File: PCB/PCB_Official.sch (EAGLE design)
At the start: 104 parts, among them IC1 MCP73871, J3 455-1750-1-ND, Q1 220mA/50V/3.5Ω, U1 TPS63070, U2 STM32F767ZIT6, U3 STM32L053C8T6, U4 TPS63070, U5 BATTERY-MANAGEMENT-TEMP_BQ274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

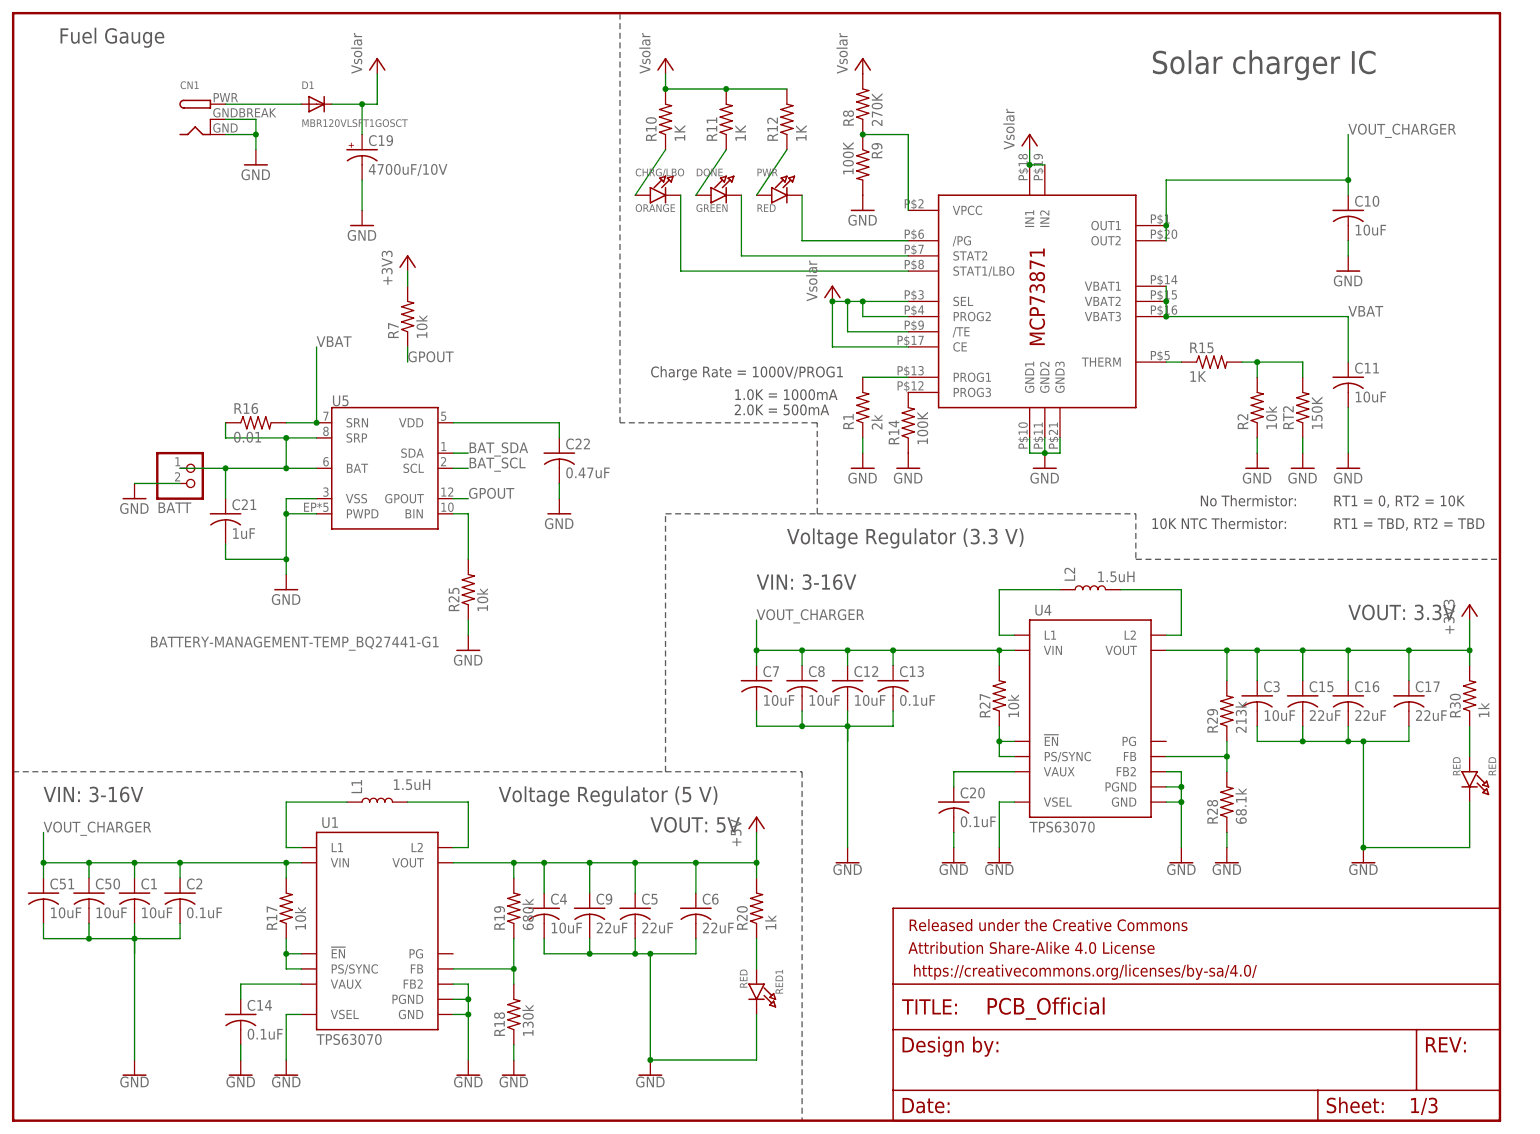
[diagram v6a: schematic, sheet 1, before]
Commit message: Passing DRU, need to fix silkscreen
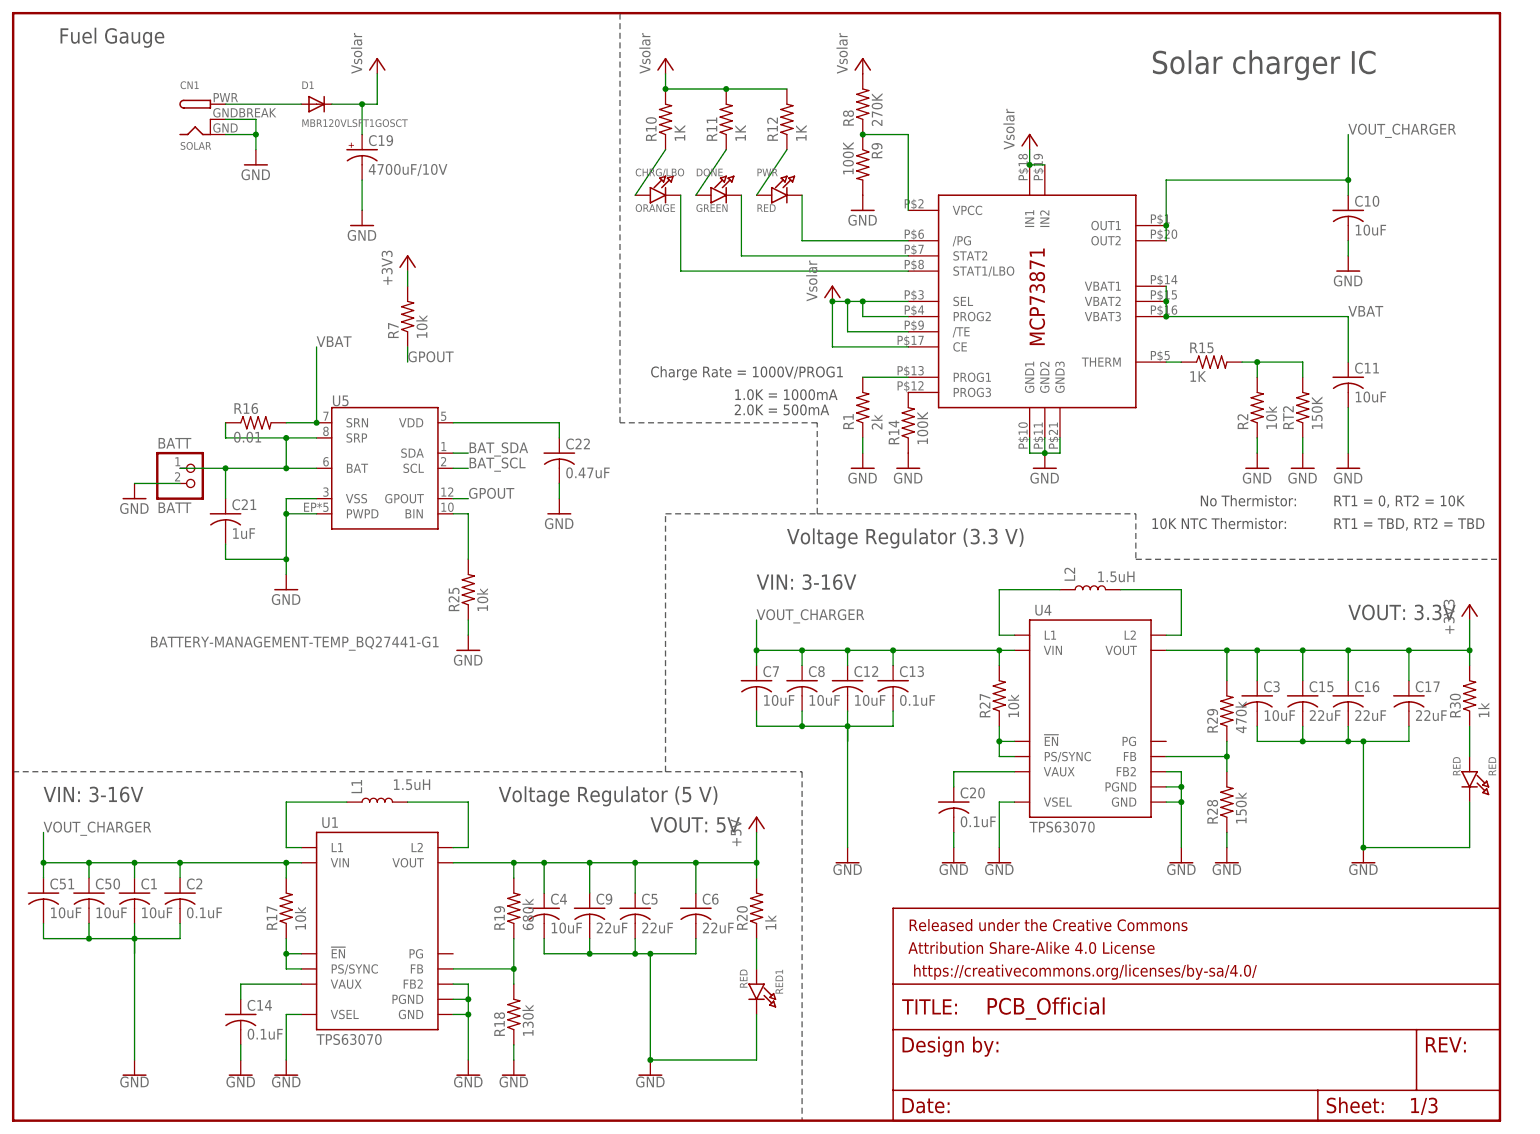
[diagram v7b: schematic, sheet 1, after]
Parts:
- BATT: value (none) -> BATT
- CN1: value (none) -> SOLAR
- J2: value (none) -> F7_PRGM
- L0_PROGRAM: value (none) -> L0_PRGM
- MCU_UART: value (none) -> MCU_UART
- R28: value 68.1k -> 150k
- R29: value 213k -> 470k
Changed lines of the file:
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@@
 <part name="GND13" library="supply1" deviceset="GND" device=""/>
 <part name="GND14" library="supply1" deviceset="GND" device=""/>
-<part name="BATT" library="adafruit" deviceset="JST_2PIN" device="-SMT-RA"/>
+<part name="BATT" library="adafruit" deviceset="JST_2PIN" device="-SMT-RA" value="BATT"/>
 <part name="GND15" library="supply1" deviceset="GND" device=""/>
 <part name="R14" library="adafruit" deviceset="R-US_" device="R0805" value="100K"/>
@@
 <part name="FRAME3" library="SparkFun-Aesthetics" library_urn="urn:adsk.eagle:library:507" deviceset="FRAME-LEDGER" device="" package3d_urn="urn:adsk.eagle:package:37121/1"/>
 <part name="U2" library="STM32F767ZIT6" deviceset="STM32F767ZIT6" device=""/>
-<part name="J2" library="SparkFun-Connectors" deviceset="CONN_05" device=""/>
+<part name="J2" library="SparkFun-Connectors" deviceset="CONN_05" device="" value="F7_PRGM"/>
 <part name="FRAME4" library="SparkFun-Aesthetics" library_urn="urn:adsk.eagle:library:507" deviceset="FRAME-A4L" device=""/>
 <part name="U3" library="STM32L053C8T6" deviceset="STM32L053C8T6" device=""/>
-<part name="L0_PROGRAM" library="SparkFun-Connectors" deviceset="CONN_05" device=""/>
+<part name="L0_PROGRAM" library="SparkFun-Connectors" deviceset="CONN_05" device="" value="L0_PRGM"/>
 <part name="U$9" library="ForestVisionParts" deviceset="LORAMODULE" device=""/>
 <part name="U$1" library="ForestVisionParts" deviceset="MIKROE_CLICK" device="LARGE"/>
@@
 <part name="C19" library="ForestVisionParts" deviceset="ADAFRUIT_CPOL-US" device="E5-13" value="4700uF/10V"/>
 <part name="GND43" library="supply1" deviceset="GND" device=""/>
-<part name="MCU_UART" library="pinhead" library_urn="urn:adsk.eagle:library:325" deviceset="PINHD-1X4" device="" package3d_urn="urn:adsk.eagle:package:22407/2"/>
+<part name="MCU_UART" library="pinhead" library_urn="urn:adsk.eagle:library:325" deviceset="PINHD-1X4" device="" package3d_urn="urn:adsk.eagle:package:22407/2" value="MCU_UART"/>
 <part name="C7" library="rcl" library_urn="urn:adsk.eagle:library:334" deviceset="C-US" device="C0603" package3d_urn="urn:adsk.eagle:package:23616/2" value="10uF"/>
 <part name="C20" library="rcl" library_urn="urn:adsk.eagle:library:334" deviceset="C-US" device="C0603" package3d_urn="urn:adsk.eagle:package:23616/2" value="0.1uF"/>
 <part name="R27" library="rcl" library_urn="urn:adsk.eagle:library:334" deviceset="R-US_" device="R0603" package3d_urn="urn:adsk.eagle:package:23555/3" value="10k"/>
-<part name="R28" library="rcl" library_urn="urn:adsk.eagle:library:334" deviceset="R-US_" device="R0603" package3d_urn="urn:adsk.eagle:package:23555/3" value="68.1k"/>
-<part name="R29" library="rcl" library_urn="urn:adsk.eagle:library:334" deviceset="R-US_" device="R0603" package3d_urn="urn:adsk.eagle:package:23555/3" value="213k"/>
+<part name="R28" library="rcl" library_urn="urn:adsk.eagle:library:334" deviceset="R-US_" device="R0603" package3d_urn="urn:adsk.eagle:package:23555/3" value="150k"/>
+<part name="R29" library="rcl" library_urn="urn:adsk.eagle:library:334" deviceset="R-US_" device="R0603" package3d_urn="urn:adsk.eagle:package:23555/3" value="470k"/>
 <part name="R30" library="rcl" library_urn="urn:adsk.eagle:library:334" deviceset="R-US_" device="R0603" package3d_urn="urn:adsk.eagle:package:23555/3" value="1k"/>
 <part name="C14" library="rcl" library_urn="urn:adsk.eagle:library:334" deviceset="C-US" device="C0603" package3d_urn="urn:adsk.eagle:package:23616/2" value="0.1uF"/>
@@
 <part name="R1" library="adafruit" library_urn="urn:adsk.eagle:library:420" deviceset="R-US_" device="R0805" package3d_urn="urn:adsk.eagle:package:6240566/1" value="2k"/>
 <part name="R2" library="adafruit" library_urn="urn:adsk.eagle:library:420" deviceset="R-US_" device="R0805" package3d_urn="urn:adsk.eagle:package:6240566/1" value="10k"/>
-<part name="CN1" library="adafruit" library_urn="urn:adsk.eagle:library:420" deviceset="DCBARREL" device="PTH" package3d_urn="urn:adsk.eagle:package:6240729/1"/>
+<part name="CN1" library="adafruit" library_urn="urn:adsk.eagle:library:420" deviceset="DCBARREL" device="PTH" package3d_urn="urn:adsk.eagle:package:6240729/1" value="SOLAR"/>
 <part name="CAMERA" library="ForestVisionParts" deviceset="TST-109-02-X-D" device=""/>
 <part name="+3V15" library="supply1" library_urn="urn:adsk.eagle:library:371" deviceset="+3V3" device=""/>

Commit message: Submitted PCB for production.
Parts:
- added F7_LED1, F7_LED2, F7_LED3, L0_LED1, L0_LED2: ORANGE, microbuilder:LED0805_NOOUTLINE
- added R13, R26, R31, R5, R6: 10k, rcl:R-US_R0805
- added R32, R33: (no value), rcl:R-US_R0805
- renumbered CHRG/LBO to CHRG, CN1 to SOLAR, RED to 3.3V, RED1 to 5V
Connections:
- new net F7_LED1: R5.2, U2PE.PE7(TIM1_ETR,DFSDM1_DATIN2,UART7_RX,QUADSPI_BK2_IO0,FMC_D4)
- new net F7_LED2: R6.2, U2PG.PG0(FMC_A10)
- new net F7_LED3: R13.2, U2PF.PF14(I2C4_SCL,DFSDM1_CKIN6,FMC_A8)
- new net L0_LED1: R26.2, U3.PB2
- new net L0_LED2: R31.2, U3.PB0
- new net N$35: F7_LED2.A, R6.1
- new net N$36: F7_LED3.A, R13.1
- new net N$37: F7_LED1.A, R5.1
- new net N$38: L0_LED2.A, R31.1
- new net N$40: L0_LED1.A, R26.1
- net +3V3: now also R32.2, R33.2
- net BAT_SCL: now also R33.1
- net BAT_SDA: now also R32.1
- net GND: now also F7_LED1.C, F7_LED2.C, F7_LED3.C, L0_LED1.C, L0_LED2.C
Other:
- moved on the sheet: U$9
